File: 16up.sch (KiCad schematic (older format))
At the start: 38 parts, among them CN1 EXPANSION_PORT, CN2 ALMOST_USERPORT, CN3 DB9_MALE, J1 ATTENTION_IN, J2 TAPE_IN, U1 GAL20V8, U102 74LS652, U2 MOS_6529, U3 MOS_6551_ACIA, U4 MAX238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

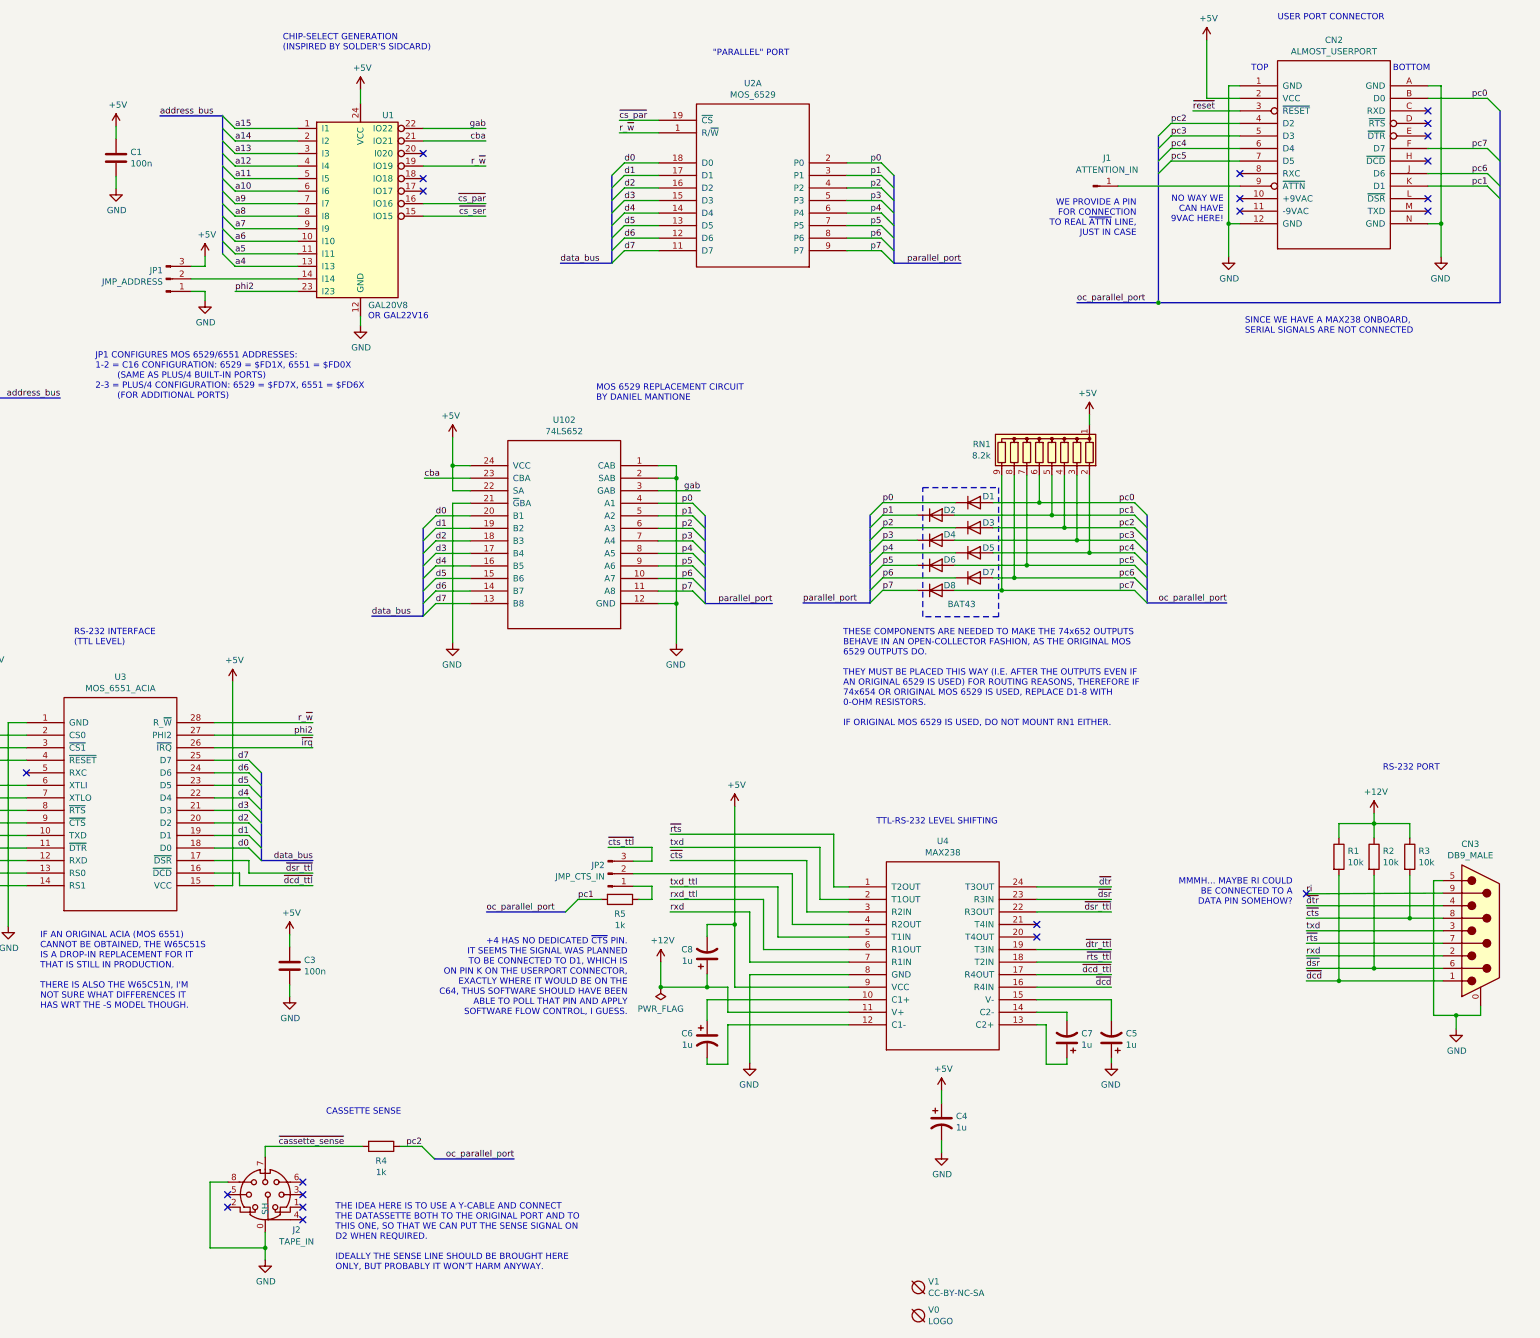
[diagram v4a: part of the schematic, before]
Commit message: Fix /CTS
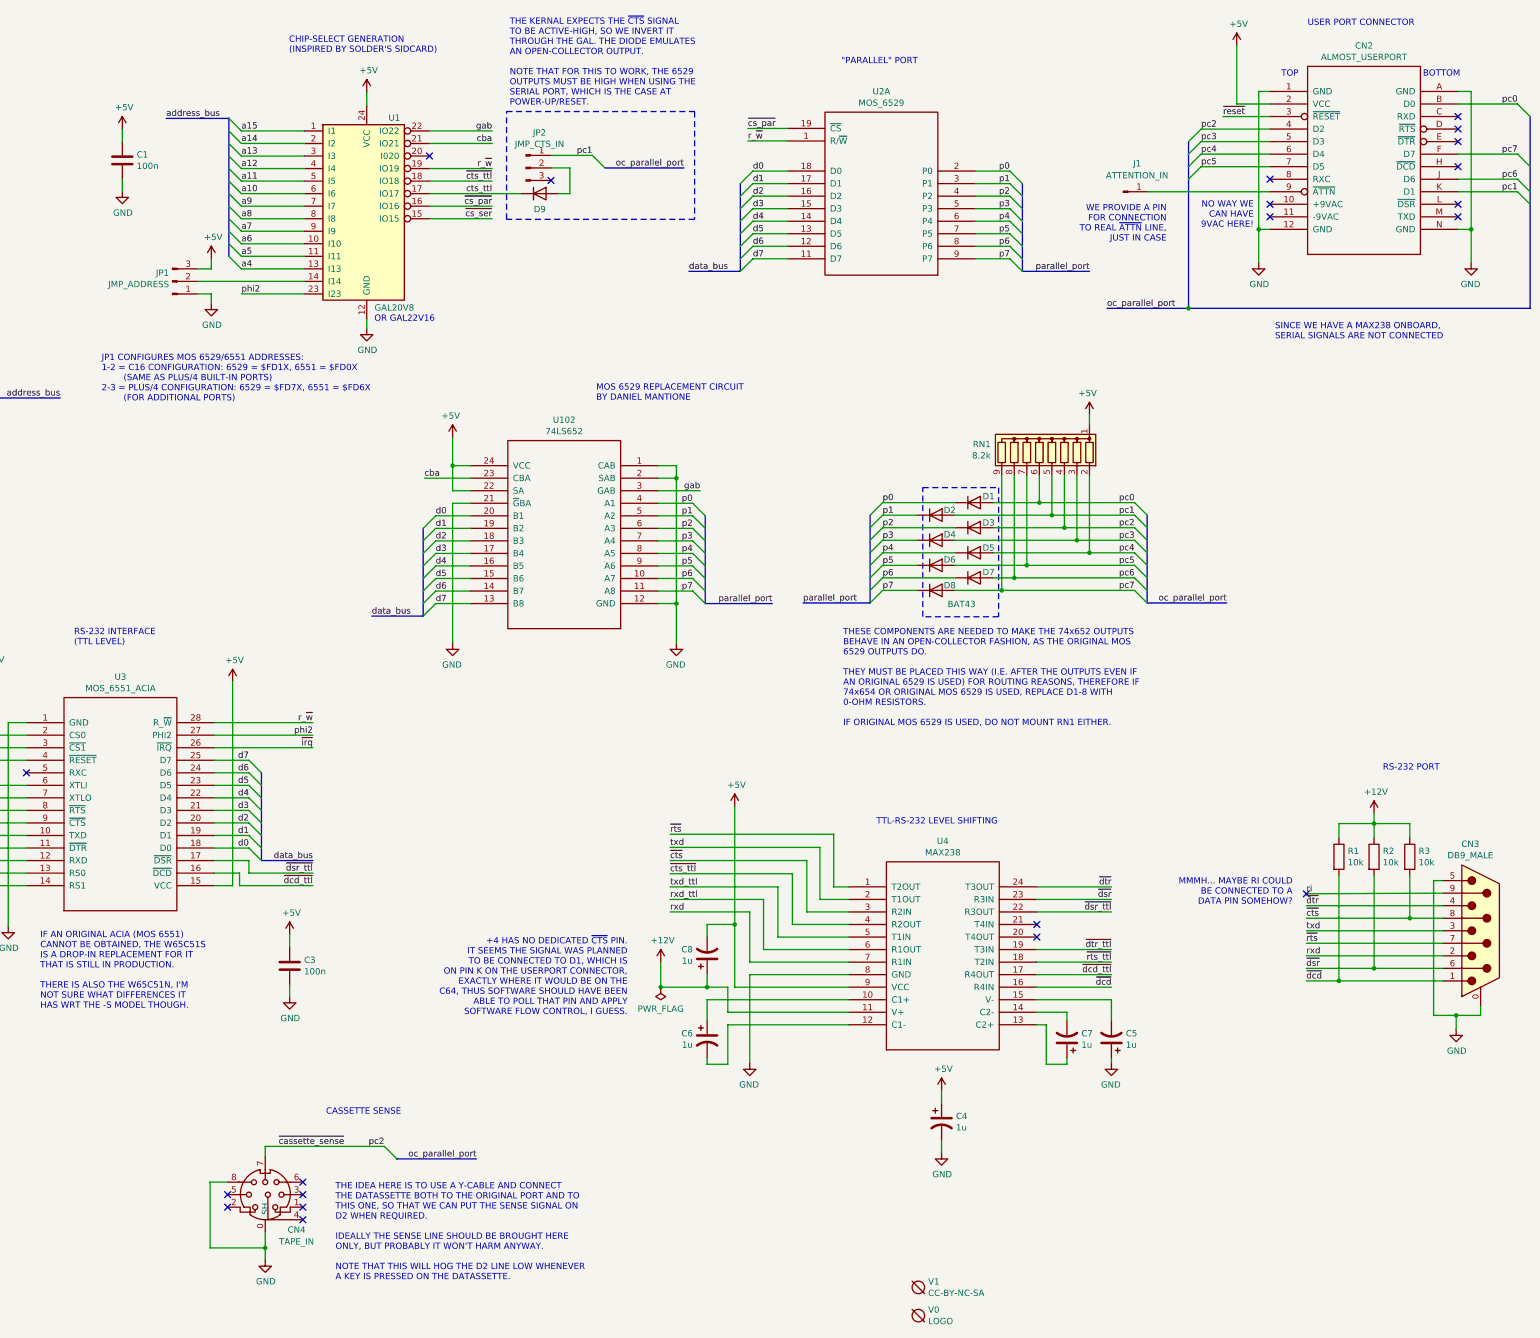
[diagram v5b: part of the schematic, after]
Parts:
- removed R4, R5: 1k, Resistor_THT:R_Axial_DIN0207_L6.3mm_D2.5mm_P2.54mm_Vertical, symbol Device:R
- added D9: BAT43, Diode_THT:D_DO-35_SOD27_P2.54mm_Vertical_KathodeUp, symbol Device:D
- renumbered J2 to CN4
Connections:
- net ~cassette_sense is gone; now on net pc2: CN4.7
- net pc1: now also JP2.1 (Pin_1)
- net ~cts_ttl: now also U1.18 (IO18), U4.4 (R2OUT); no longer JP2.3 (Pin_3)
- net at JP2.2 (Pin_2): now also D9.2 (A); no longer U4.4 (R2OUT)
- net cts_ttl: now reaches U1.17 (IO17)
- net cts_ttl: now also D9.1 (K)
- no-connect marks 37 -> 36
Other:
- note added: "THE IDEA HERE IS TO USE A Y-CABLE AND CONNECT\nTHE DATASSETTE BOTH TO THE ORIGINAL PORT AND TO\nTHIS ONE, SO THAT WE CAN PUT THE SENSE SIGNAL ON\nD2 WHEN REQUIRED.\n\nIDEALLY THE SENSE LINE SHOULD BE BROUGHT HERE\nONLY, BUT PROBABLY IT WON'T HARM ANYWAY.\n\nNOTE THAT THIS WILL HOG THE D2 LINE LOW WHENEVER\nA KEY IS PRESSED ON THE DATASSETTE."
- note added: "THE KERNAL EXPECTS THE ~CTS~ SIGNAL\nTO BE ACTIVE-HIGH, SO WE INVERT IT\nTHROUGH THE GAL. THE DIODE EMULATES\nAN OPEN-COLLECTOR OUTPUT.\n\nNOTE THAT FOR THIS TO WORK, THE 6529\nOUTPUTS MUST BE HIGH WHEN USING THE\nSERIAL PORT, WHICH IS THE CASE AT\nPOWER-UP/RESET."
- note removed: "THE IDEA HERE IS TO USE A Y-CABLE AND CONNECT\nTHE DATASSETTE BOTH TO THE ORIGINAL PORT AND TO\nTHIS ONE, SO THAT WE CAN PUT THE SENSE SIGNAL ON\nD2 WHEN REQUIRED.\n\nIDEALLY THE SENSE LINE SHOULD BE BROUGHT HERE\nONLY, BUT PROBABLY IT WON'T HARM ANYWAY.\n\n"
- moved on the sheet: C1, CN2, J1, JP1, JP2, U1, U2A

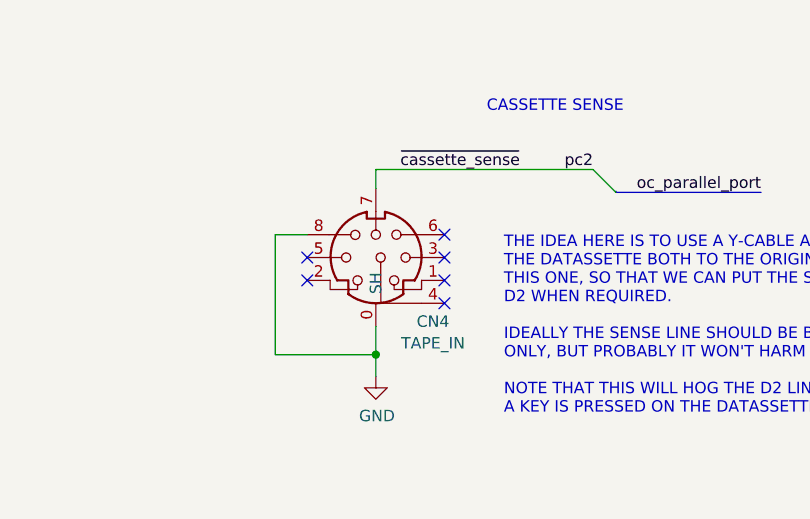
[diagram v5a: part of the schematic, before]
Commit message: Use better MiniDIN-7 footprint The former was actually a MiniDIN-8...
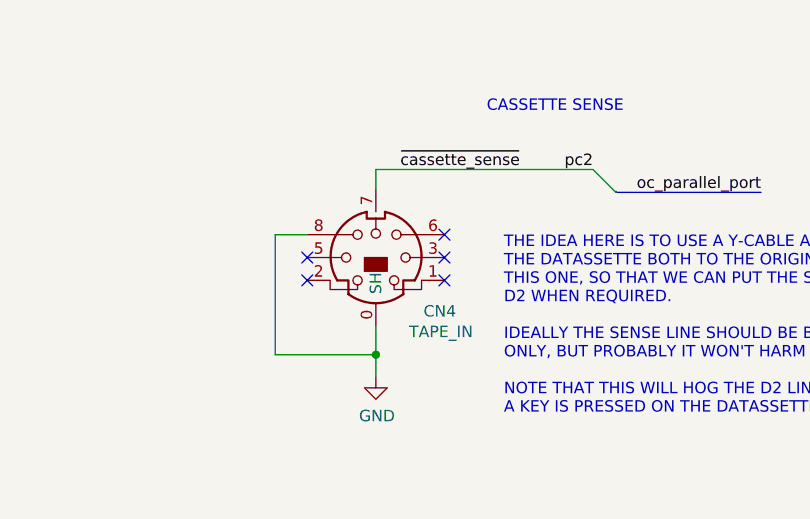
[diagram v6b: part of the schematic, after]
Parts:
- removed CN4: TAPE_IN, 16up:Connector_Mini-DIN_Female_8Pin_2rows, symbol mini-din-8:Mini-DIN-8
- added CN4: TAPE_IN, 16up:KMDGX-7S-BS, symbol mini-din-7:Mini-DIN-7
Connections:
- net GND: now also CN4.0 (SH), CN4.8
- net pc2: now also CN4.7
- no-connect marks 36 -> 35
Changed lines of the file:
@@
 Wire Wire Line
 	11965 4540 12725 4540
-$Comp
-L mini-din-8:Mini-DIN-8 CN4
-U 1 1 63742584
-P 5790 10060
-F 0 "CN4" H 6040 9780 50  0000 C CNN
-F 1 "TAPE_IN" H 6040 9685 50  0000 C CNN
-F 2 "16up:Connector_Mini-DIN_Female_8Pin_2rows" V 5780 10050 50  0001 C CNN
-F 3 "http://service.powerdynamics.com/ec/Catalog17/Section%2011.pdf" V 5780 10050 50  0001 C CNN
-	1    5790 10060
-	1    0    0    -1
-$EndComp
 Wire Wire Line
 	5490 9960 5350 9960
@@
 	5790 10485 5790 10580
 Connection ~ 5790 10485
-NoConn ~ 6090 10260
 NoConn ~ 6090 10160
 NoConn ~ 6090 10060
@@
 Wire Bus Line
 	5500 1470 5500 2575
+$Comp
+L mini-din-7:Mini-DIN-7 CN4
+U 1 1 63BBDF9F
+P 5790 10060
+F 0 "CN4" H 6070 9825 50  0000 C CNN
+F 1 "TAPE_IN" H 6075 9735 50  0000 C CNN
+F 2 "16up:KMDGX-7S-BS" V 5780 10050 50  0001 C CNN
+F 3 "" V 5780 10050 50  0001 C CNN
+	1    5790 10060
+	1    0    0    -1
+$EndComp
 $EndSCHEMATC

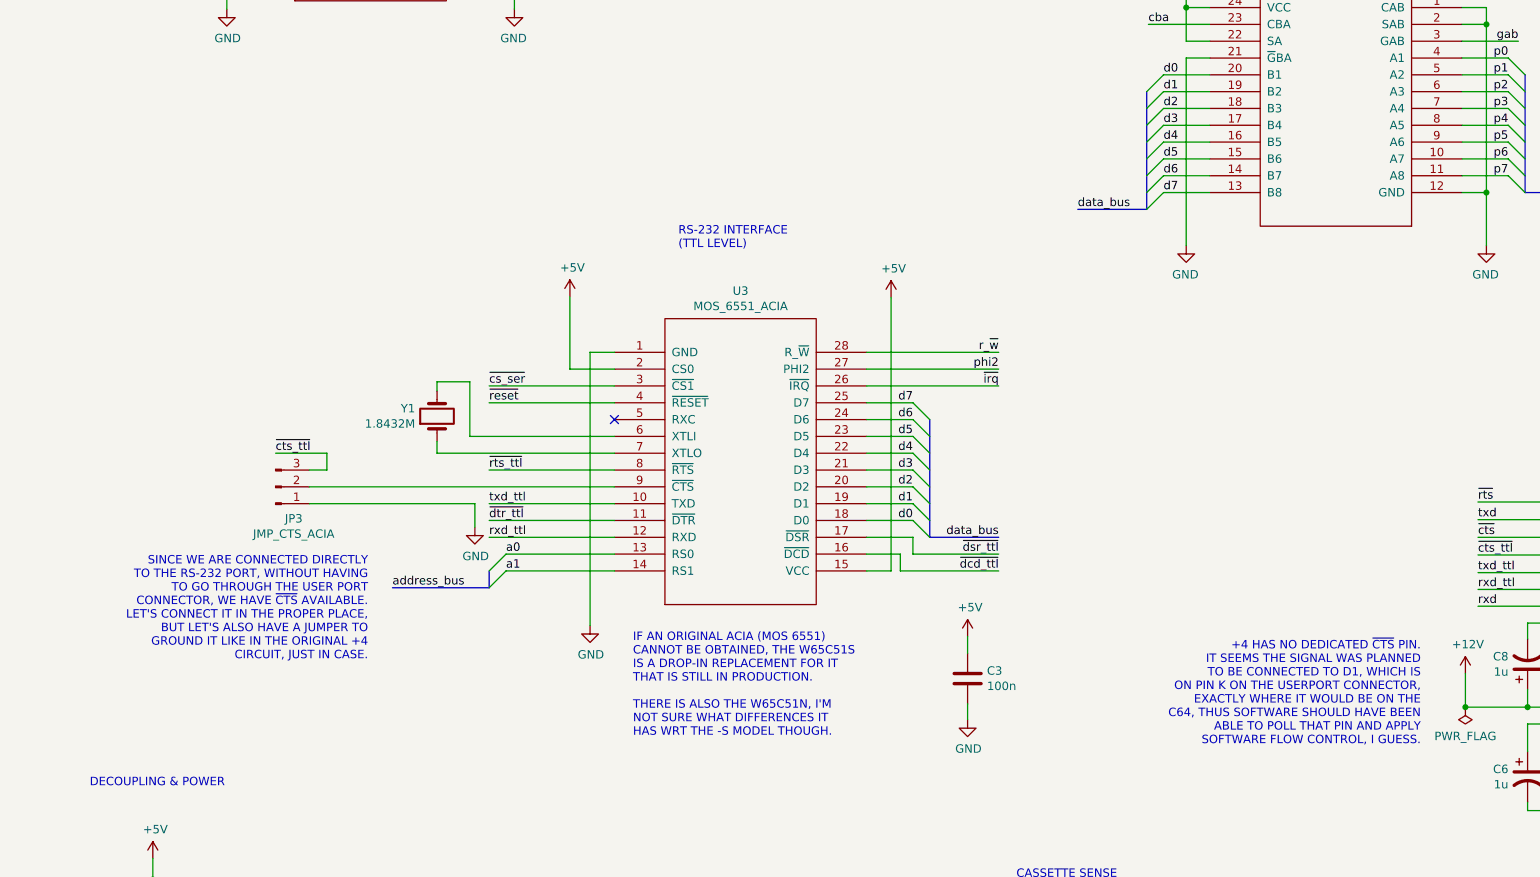
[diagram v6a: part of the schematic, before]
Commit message: Improve ground plane
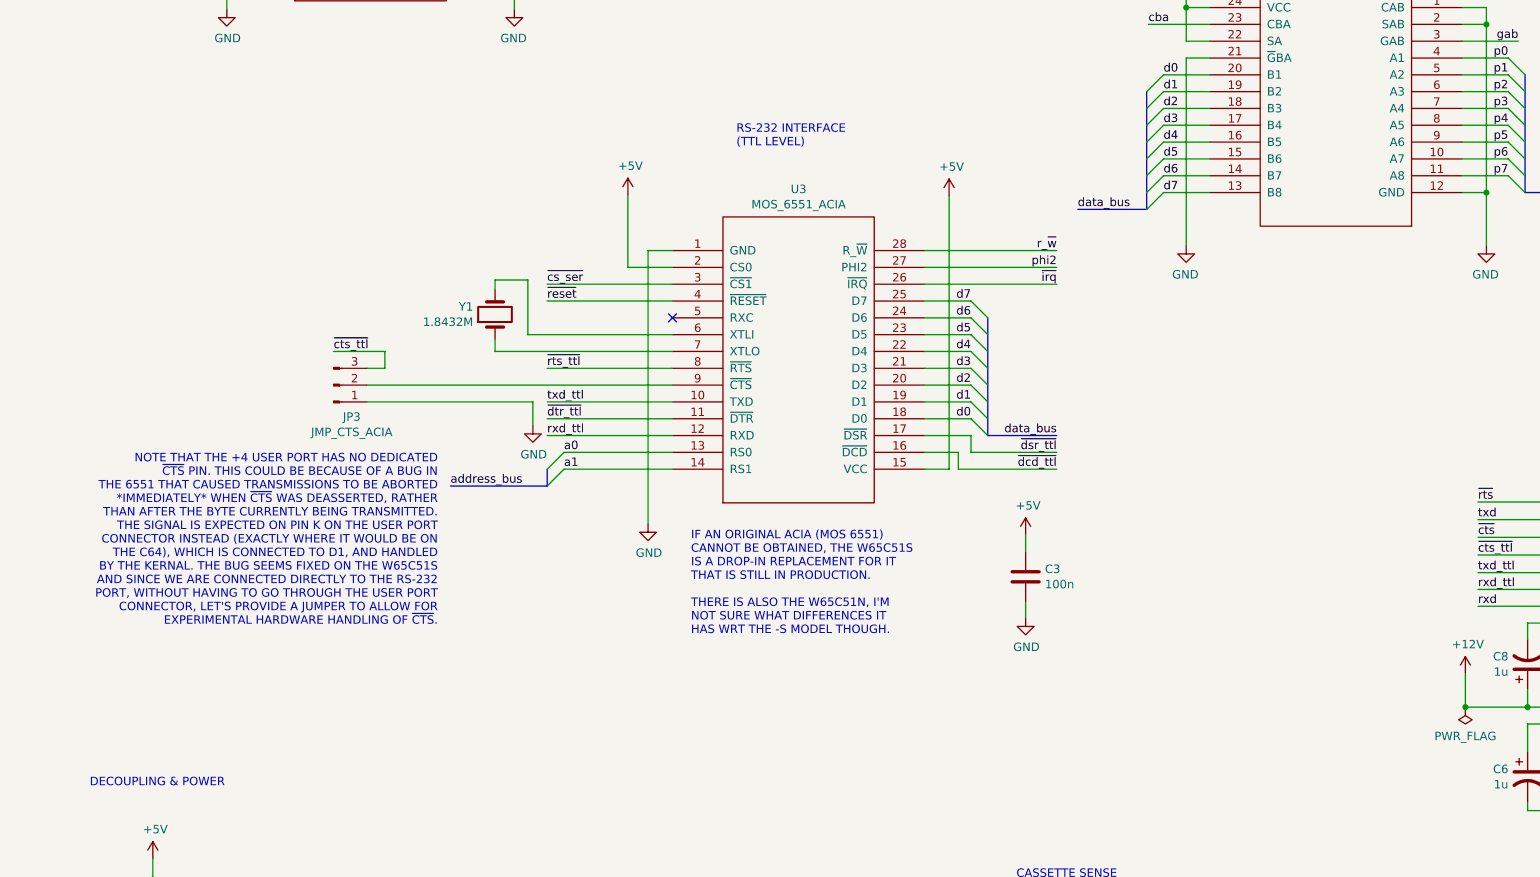
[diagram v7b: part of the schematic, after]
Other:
- note added: "NOTE THAT THE +4 USER PORT HAS NO DEDICATED\n~CTS~ PIN. THIS COULD BE BECAUSE OF A BUG IN\nTHE 6551 THAT CAUSED TRANSMISSIONS TO BE ABORTED\n*IMMEDIATELY* WHEN ~CTS~ WAS DEASSERTED, RATHER\nTHAN AFTER THE BYTE CURRENTLY BEING TRANSMITTED.\nTHE SIGNAL IS EXPECTED ON PIN K ON THE USER PORT\nCONNECTOR INSTEAD (EXACTLY WHERE IT WOULD BE ON\nTHE C64), WHICH IS CONNECTED TO D1, AND HANDLED\nBY THE KERN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"
- note removed: "+4 HAS NO DEDICATED ~CTS~ PIN.\nIT SEEMS THE SIGNAL WAS PLANNED\nTO BE CONNECTED TO D1, WHICH IS\nON PIN K ON THE USERPORT CONNECTOR,\nEXACTLY WHERE IT WOULD BE ON THE\nC64, THUS SOFTWARE SHOULD HAVE BEEN\nABLE TO POLL THAT PIN AND APPLY\nSOFTWARE FLOW CONTROL, I GUESS."
- note removed: "SINCE WE ARE CONNECTED DIRECTLY\nTO THE RS-232 PORT, WITHOUT HAVING\nTO GO THROUGH THE USER PORT\nCONNECTOR, WE HAVE ~CTS~ AVAILABLE.\nLET'S CONNECT IT IN THE PROPER PLACE,\nBUT LET'S ALSO HAVE A JUMPER TO\nGROUND IT LIKE IN THE ORIGINAL +4\nCIRCUIT, JUST IN CASE."
- moved on the sheet: C3, JP3, U3, Y1

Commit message: Only support 74x654 as 6529 replacement
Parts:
- removed D1, D2, D3, D4, D5, D6, D7, D8: BAT43, Diode_THT:D_DO-35_SOD27_P2.54mm_Vertical_KathodeUp, symbol Device:D
- renumbered D9 to D1
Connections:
- net pc2 is gone; now on net p2: CN2.4 (D2), CN4.7, RN1.4 (R3)
- net pc5 is gone; now on net p5: CN2.7 (D5), RN1.7 (R6)
- net pc6 is gone; now on net p6: CN2.J (D6), RN1.8 (R7)
- net pc7 is gone; now on net p7: CN2.F (D7), RN1.9 (R8)
- net p0: now also CN2.B (D0), RN1.2 (R1)
- net p1: now also CN2.K (D1), JP2.1 (Pin_1), RN1.3 (R2)
- net p3: now also CN2.5 (D3), RN1.5 (R4)
- net p4: now also CN2.6 (D4), RN1.6 (R5)
- removed net pc0: CN2.B (D0), RN1.6 (R5)
- removed net pc1: CN2.K (D1), JP2.1 (Pin_1), RN1.5 (R4)
- removed net pc3: CN2.5 (D3), RN1.3 (R2)
- removed net pc4: CN2.6 (D4), RN1.2 (R1)
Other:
- moved on the sheet: RN1
